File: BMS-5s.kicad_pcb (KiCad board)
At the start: 2 copper layers, 108 x 57.5 mm, 158 parts, among them J2 UEXT, P1 Conn_Switch-N-Sense, P2 CONN_01X06, P3 ON/OFF, P4 USB_Micro-B, P5 CONN_01X02, P6 CONN_01X02, P7 CONN_01X02, Q1 DMN2004K, Q2 BSS84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

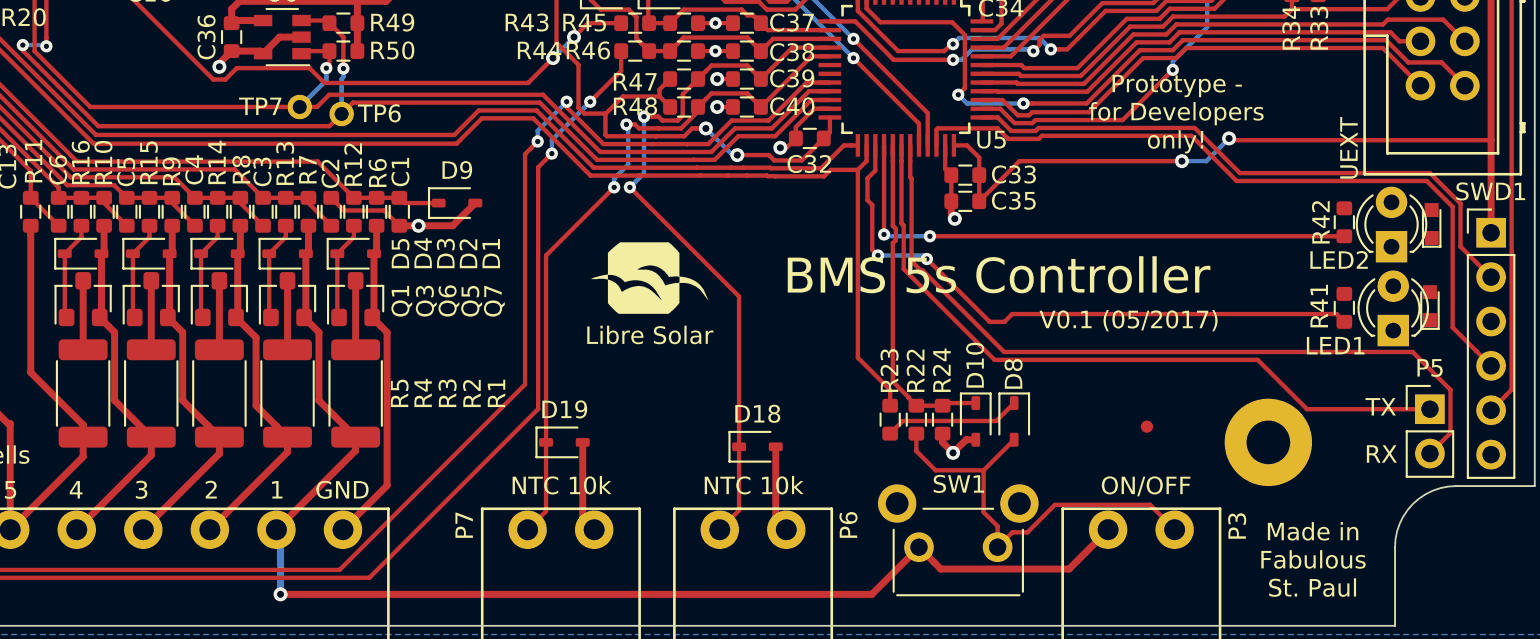
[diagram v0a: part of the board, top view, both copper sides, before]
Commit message: Small fixes for final gerber export (DRU check passed)
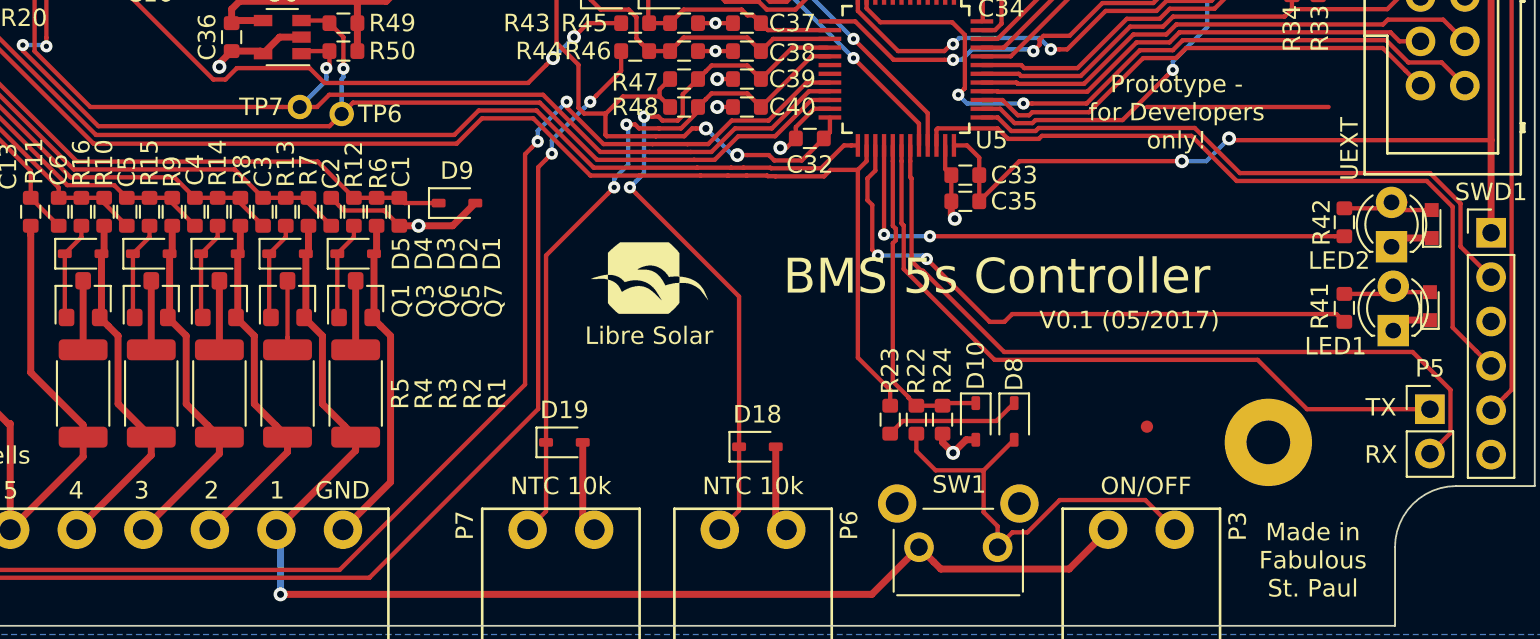
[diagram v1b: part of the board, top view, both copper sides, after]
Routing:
- net (no net): track 0.00 -> 10.4 mm
- net Net-(LED2-Pad2): track 0.48 -> 5.80 mm
- net Net-(LED1-Pad2): track 0.00 -> 5.22 mm
- net GND: track 114.2 -> 119.0 mm
